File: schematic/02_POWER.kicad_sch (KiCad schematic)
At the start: 29 parts, among them J1 VIN_3V0-5V5, SW1 DISABLE, U2 TLV73330PDBV

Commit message: Schematic: GNSS COEX0 bias switch, 3.3V VDD_GPIO, DNP RF shunts
- Add U3 TPS22919DCKR on 04_GNSS (COEX0-gated bias); FB5 0402
- Swap U2 to TLV73333 (3.3 V VDD_GPIO); DNP Class-C shunt caps
- Quarantine leftover schematics/; remove stale ERC rpt
- Add PM/DFM/RF/schematic/layout review docs under docs/
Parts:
- U2: value TLV73330PDBV -> TLV73333PDBV; symbol Regulator_Linear:TLV73330PDBV -> Regulator_Linear:TLV73333PDBV
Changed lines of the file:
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@@
 	)
 	(symbol
-		(lib_id "Regulator_Linear:TLV73330PDBV")
+		(lib_id "Regulator_Linear:TLV73333PDBV")
 		(at 63.5 101.6 0)
 		(unit 1)
@@
 			)
 		)
-		(property "Value" "TLV73330PDBV"
+		(property "Value" "TLV73333PDBV"
 			(at 63.5 104.14 0)
 			(show_name no)
@@
 			)
 		)
-		(property "Description" "300mA Capacitor-Free Low Dropout Voltage Regulator, Fixed Output 3.0V, SOT-23-5"
+		(property "Description" "300mA Capacitor-Free Low Dropout Voltage Regulator, Fixed Output 3.3V, SOT-23-5"
 			(at 63.5 101.6 0)
 			(hide yes)

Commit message: Schematic: add C40 100nF X7R on SIM_1V8 at U1; D3-D7 values restored (Function field); D7 DNP; ERC 0 errors
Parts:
- D3: value POWER -> Green LED; Function (none) -> POWER; MPN (none) -> KP-2012SGC; Manufacturer (none) -> Kingbright
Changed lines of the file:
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@@
 			)
 		)
-		(property "Value" "POWER"
+		(property "Value" "Green LED"
 			(at 38.1 78.74 0)
 			(show_name no)
 			(do_not_autoplace no)
+			(effects
+				(font
+					(size 1.27 1.27)
+				)
+			)
+		)
+		(property "Function" "POWER"
+			(at 38.1 81.28 0)
+			(show_name no)
+			(do_not_autoplace no)
+			(effects
+				(font
+					(size 1.27 1.27)
+				)
+			)
+		)
+		(property "Manufacturer" "Kingbright"
+			(at 38.1 78.74 0)
+			(hide yes)
+			(show_name no)
+			(do_not_autoplace no)
+			(effects
+				(font
+					(size 1.27 1.27)
+				)
+			)
+		)
+		(property "MPN" "KP-2012SGC"
+			(at 38.1 78.74 0)
+			(hide yes)
+			(show_name no)
+			(do_not_autoplace no)

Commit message: Exclude JP1, JP2, TP1-TP20 from BOM (attrs only, sch+pcb)
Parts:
- JP1: now left out of the parts list
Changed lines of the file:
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@@
 		(unit 1)
 		(exclude_from_sim no)
-		(in_bom yes)
+		(in_bom no)
 		(on_board yes)
 		(dnp no)

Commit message: v2: simplify to UART modem module (J20 host header, LXC translators); remove J1, J3, J6, J9-J18, optional parts
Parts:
- removed J1: VIN_3V0-5V5, Connector_PinHeader_2.54mm:PinHeader_1x02_P2.54mm_Vertical, symbol Connector_Generic:Conn_01x02
- removed JP1: I_MEAS, Jumper:SolderJumper-2_P1.3mm_Open_RoundedPad1.0x1.5mm, symbol Jumper:SolderJumper_2_Open
- removed R2: 0.05, Resistor_SMD:R_1206_3216Metric, symbol Device:R
- removed SW1: DISABLE, Button_Switch_SMD:SW_SPST_CK_KXT3, symbol Switch:SW_Push
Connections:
- net VIN_FILT is gone; now on net VDD_nRF: C1.1, C2.1, FB4.2

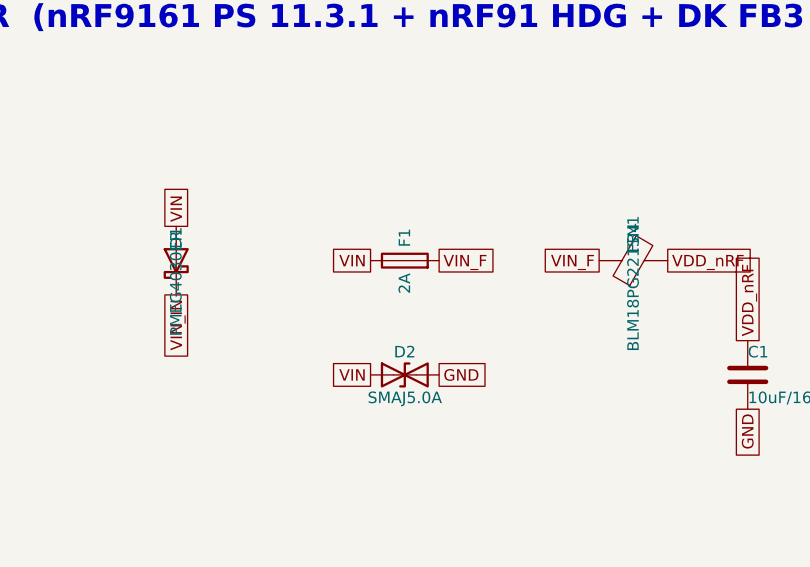
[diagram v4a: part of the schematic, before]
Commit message: v2 BOM: apply footprint-consistent MPNs + LCSC IDs, JLC BOM, audit reports (U4 footprint pending Layout)
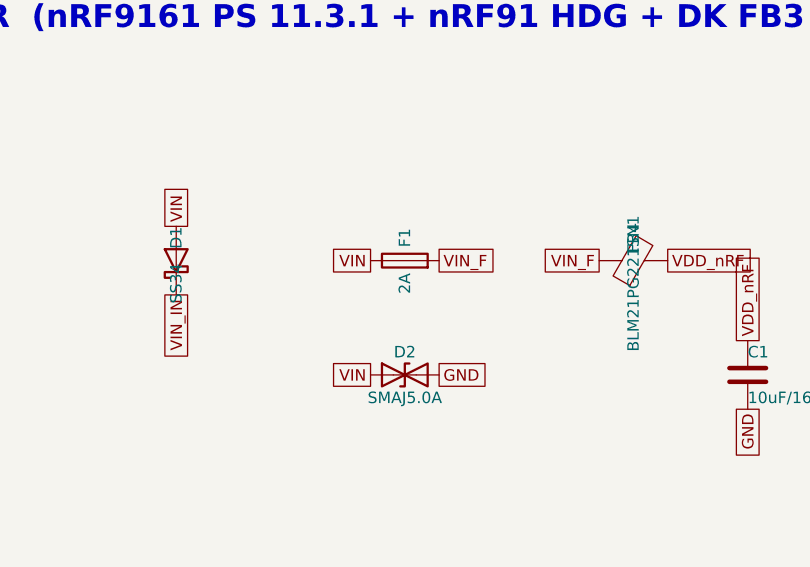
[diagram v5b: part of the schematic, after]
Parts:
- C1: LCSC (none) -> C1713; MPN (none) -> CL21A106KOQNNNE; Manufacturer (none) -> Samsung Electro-Mechanics
- C10, C6: LCSC (none) -> C710722; MPN (none) -> GJM0335C1E150JB01D; Manufacturer (none) -> Murata
- C11, C13, C4, C8: LCSC (none) -> C335105; MPN (none) -> GRM155R61A475MEAAD; Manufacturer (none) -> Murata
- C12, C14, C5, C9: LCSC (none) -> C76934; MPN (none) -> GRM033R61A104KE15D; Manufacturer (none) -> Murata
- C2: LCSC (none) -> C1525; MPN (none) -> CL05B104KO5NNNC; Manufacturer (none) -> Samsung Electro-Mechanics
- C3, C7: LCSC (none) -> C124129; MPN (none) -> GRM21BR61A476ME15L; Manufacturer (none) -> Murata
- D1: value PMEG4030ER -> SS34; LCSC (none) -> C8678; MPN (none) -> SS34; Manufacturer (none) -> MDD (Microdiode)
- D2: LCSC (none) -> C10758; MPN (none) -> SMAJ5.0A; Manufacturer (none) -> RUILON
- D3: LCSC (none) -> C125098; MPN KP-2012SGC -> LTST-C191KGKT; Manufacturer Kingbright -> Lite-On
- F1: LCSC (none) -> C187611; MPN (none) -> 0468002.NRHF; Manufacturer (none) -> Littelfuse
- FB1, FB2, FB3: LCSC (none) -> C88980; MPN (none) -> BLM18KG221SN1D; Manufacturer (none) -> Murata
- FB4: value BLM18PG221SN1 -> BLM21PG221SN1; LCSC (none) -> C85840; MPN (none) -> BLM21PG221SN1D; Manufacturer (none) -> Murata
- R1: LCSC (none) -> C106225; MPN (none) -> RC0201FR-0710KL; Manufacturer (none) -> Yageo
- R3: LCSC (none) -> C11702; MPN (none) -> 0402WGF1001TCE; Manufacturer (none) -> UNI-ROYAL
- U2: LCSC (none) -> C134139; MPN (none) -> TLV73333PDBVR; Manufacturer (none) -> Texas Instruments
